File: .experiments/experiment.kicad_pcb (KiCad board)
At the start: 2 copper layers, 140 x 90 mm, 39 parts, among them J1 USB_C, J2 Output, J3 Debug, Q1 FS8205A, U1 USBLC6-2SC6, U2 BQ24072, U3 HY2113-KB5B, U4 MT3608, U5 AP2112K-3.3, U6 LN61CN3302MR-G

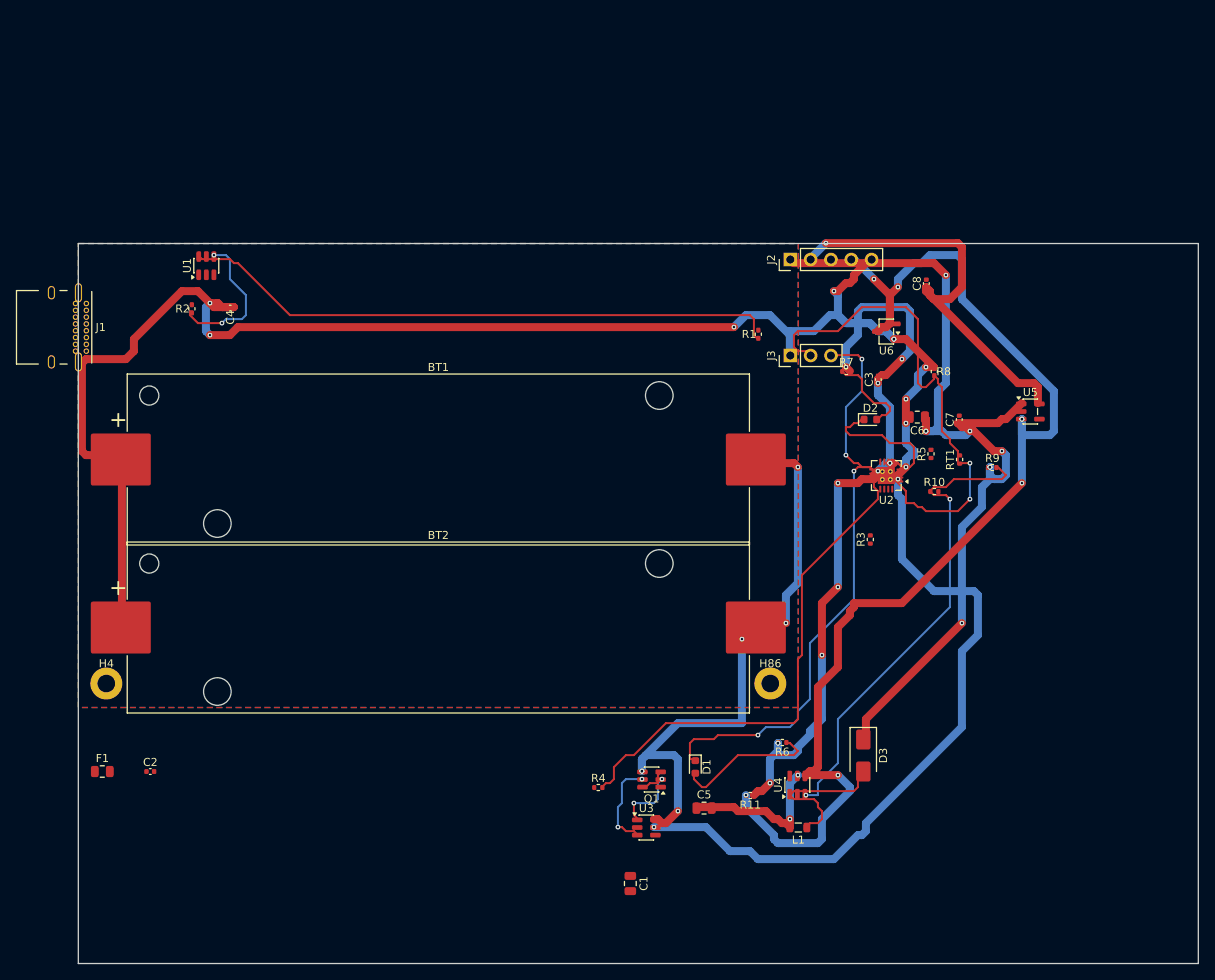
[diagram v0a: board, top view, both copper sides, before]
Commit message: 35-round experiment: best score 25.33, improved routing params
Router and conflict resolution tuning from autonomous optimization loop.
Best config: clearance=0.2051mm, cooling_factor=0.9735, existing_trace_cost=200.0

Co-Authored-By: Claude Opus 4.6 <noreply@anthropic.com>
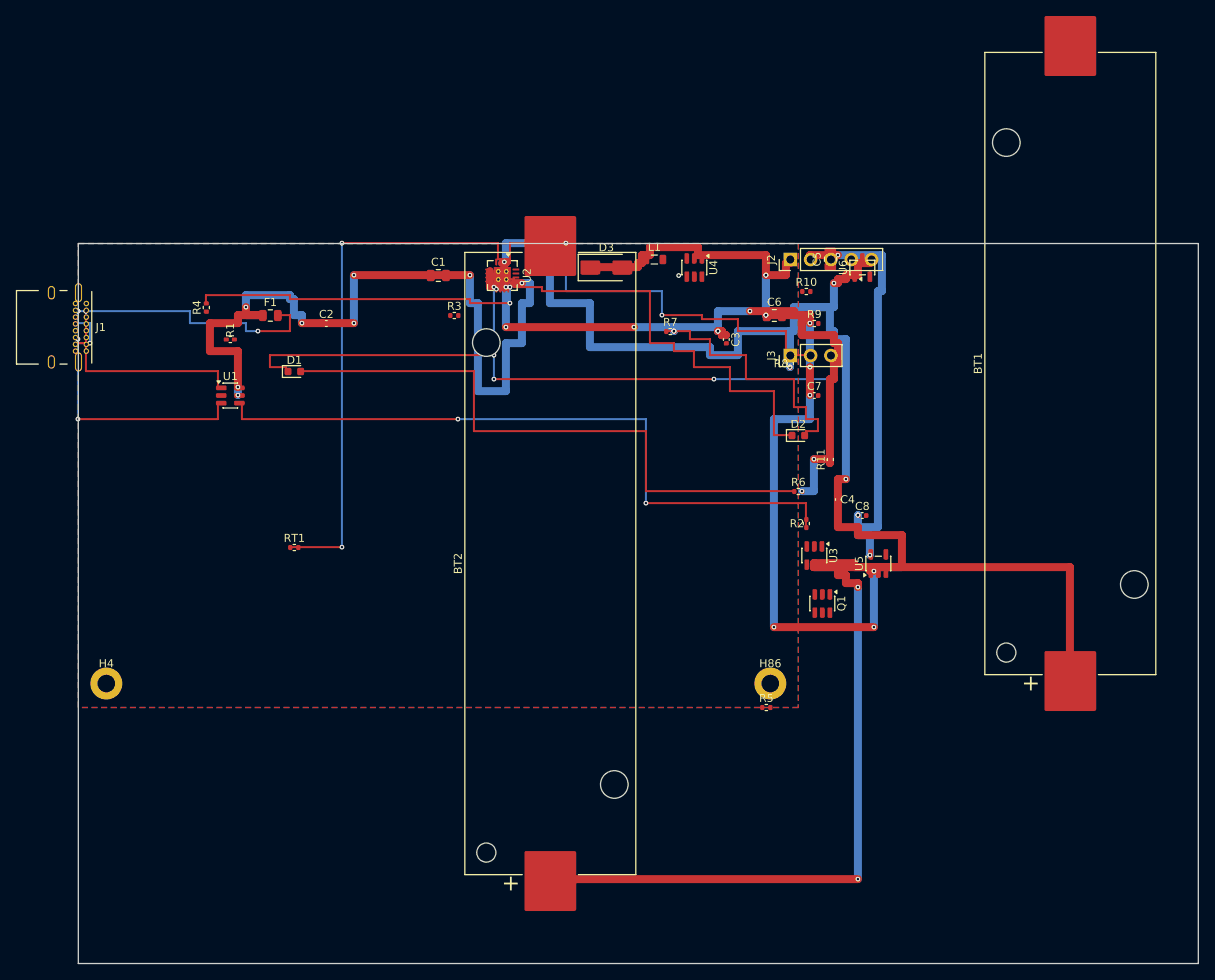
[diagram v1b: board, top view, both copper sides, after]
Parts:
- moved RT1 83.9 mm to (27.0, 38.0), turned to 0 degrees
- moved R2 81.4 mm to (91.0, 35.0)
- moved BT1 79.9 mm to (124.0, 15.0), turned to 90 degrees
- moved C1 79.7 mm to (45.0, 4.00), turned to 0 degrees
- moved C4 79.7 mm to (95.0, 32.0), turned to -90 degrees
- moved R4 77.5 mm to (16.0, 8.00), turned to 90 degrees
- moved L1 73.2 mm to (72.0, 2.00), turned to 0 degrees
- moved C5 70.4 mm to (94.0, 1.95), turned to 90 degrees
- moved D1 70.4 mm to (27.0, 16.0), turned to 0 degrees
- moved D3 68.9 mm to (66.0, 3.00), turned to 0 degrees
- moved R1 66.0 mm to (19.0, 12.0), turned to 0 degrees
- moved U4 66.0 mm to (77.0, 3.00), turned to -90 degrees
- moved F1 60.7 mm to (24.0, 9.00)
- moved C2 60.2 mm to (31.0, 10.0)
- moved R3 59.1 mm to (47.0, 9.00), turned to 0 degrees
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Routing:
- net /EN: track 149.0 -> 0.00 mm, vias 8 -> 0
- net /VBUS: track 0.00 -> 99.5 mm, vias 0 -> 8
- net Net-(R1-Pad1): track 75.5 -> 0.00 mm
- net /CELL_NEG: track 75.5 -> 0.00 mm, vias 6 -> 0
- net Net-(R2-Pad1): track 18.4 -> 86.5 mm
- net /NTC_SENSE: track 62.8 -> 123.0 mm, vias 2 -> 4
- net Net-(U4-FB): track 60.0 -> 0.00 mm, vias 2 -> 0
- net Net-(D1-A): track 17.7 -> 76.5 mm
- net Net-(F1-Pad2): track 0.00 -> 40.5 mm, vias 0 -> 6
- net Net-(D2-K): track 18.7 -> 57.5 mm
- net Net-(J1-CC2): track 0.00 -> 30.0 mm, vias 0 -> 2
- net Net-(J1-CC1): track 0.00 -> 26.0 mm
- net /CHG_N: track 75.4 -> 99.5 mm, vias 4 -> 6
- net Net-(D2-A): track 11.2 -> 33.5 mm
- net Net-(U2-ILIM): track 62.7 -> 42.0 mm, vias 0 -> 2
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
